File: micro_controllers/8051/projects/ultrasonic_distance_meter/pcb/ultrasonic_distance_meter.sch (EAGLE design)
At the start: 25 parts, among them IC1 AT89S51, IC2 7805TV

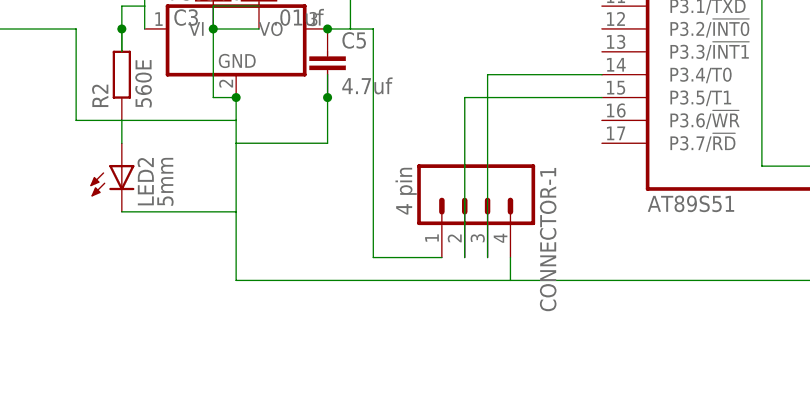
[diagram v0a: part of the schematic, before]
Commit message: 
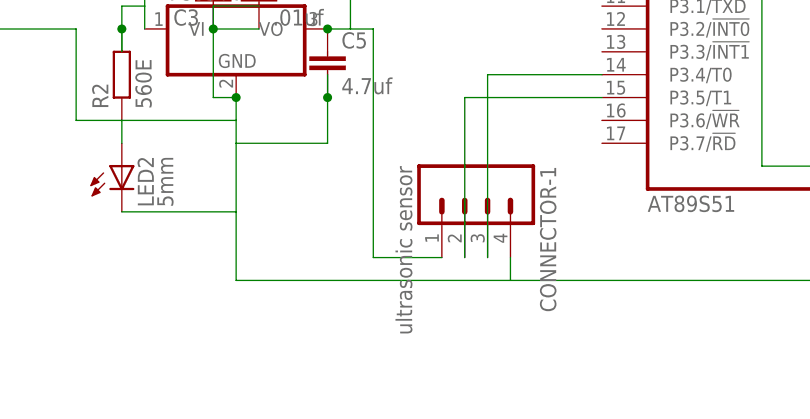
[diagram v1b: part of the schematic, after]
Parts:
- CONNECTOR-1: value 4 pin -> ultrasonic sensor
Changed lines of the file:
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@@
 <part name="S2" library="switch-dil" deviceset="DP02" device="" value="push switch"/>
 <part name="C6" library="capacitor-wima" deviceset="C" device="2.5/6" value="0.1uf"/>
-<part name="CONNECTOR-1" library="con-amp-quick" deviceset="M04" device="" value="4 pin">
+<part name="CONNECTOR-1" library="con-amp-quick" deviceset="M04" device="" value="ultrasonic sensor">
 <attribute name="MF" value=""/>
 <attribute name="MPN" value=""/>
